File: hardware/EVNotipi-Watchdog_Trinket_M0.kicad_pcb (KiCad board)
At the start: 2 copper layers, 25 x 34 mm, 11 parts, among them J1 Conn_Left, J2 Conn_Right, J3 Conn_Pi, J4 Conn_Pwr, J5 Conn_01x04_Male, Q1 BS170, Q2 IRF5305, U1 TSR_2-2450

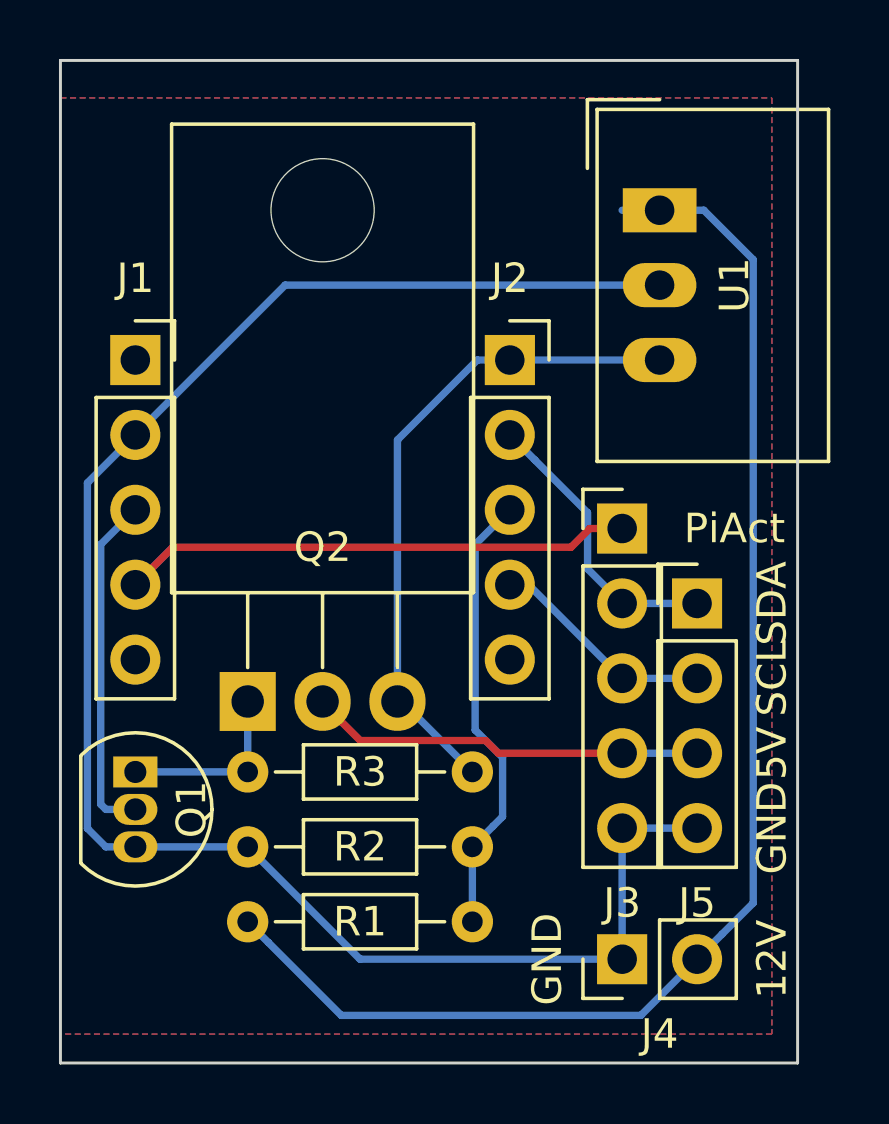
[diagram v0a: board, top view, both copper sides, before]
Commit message: Beef up current carrying traces
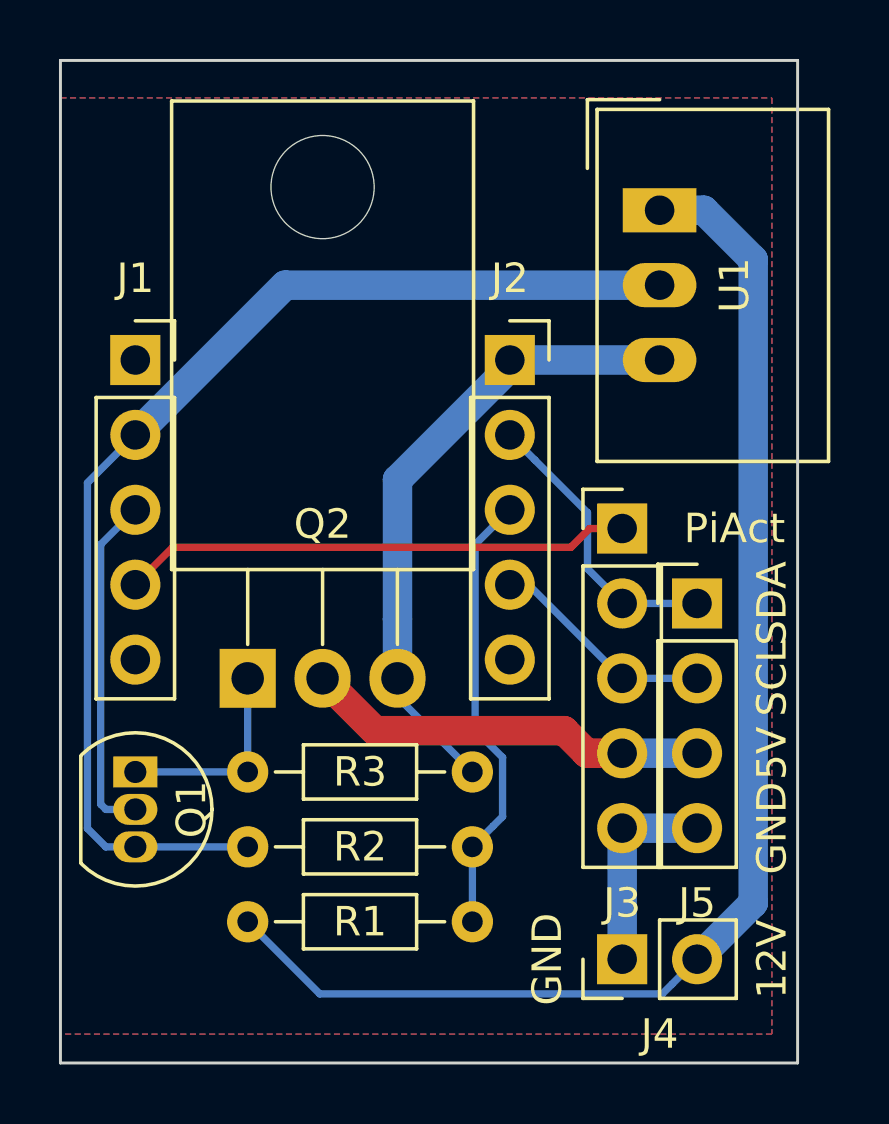
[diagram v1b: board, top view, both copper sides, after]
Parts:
- moved Q2 0.78 mm to (61.0, 51.4)
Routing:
- net GND: track 60.9 -> 46.6 mm
- net VCC12V: track 46.2 -> 45.1 mm
- net Net-(Q1-Pad1): track 6.20 -> 6.98 mm
- net VCC5V: track 22.4 -> 21.7 mm
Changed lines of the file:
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@@
     (thickness 1.6)
     (drawings 11)
-    (tracks 59)
+    (tracks 54)
     (zones 0)
     (modules 11)
@@
   (setup
     (last_trace_width 0.25)
+    (user_trace_width 1)
     (trace_clearance 0.2)
     (zone_clearance 0.508)
@@
   )
   (module Package_TO_SOT_THT:TO-220-3_Horizontal_TabDown (layer F.Cu)
-    (at 60.96 52.22)
+    (at 60.96 51.435)
     (descr "TO-220-3, Horizontal, RM 2.54mm, see https://www.vishay.com/docs/66542/to-220-1.pdf")
     (tags "TO-220-3 Horizontal RM 2.54mm")
@@
   (segment (start 55.974999 46.895001) (end 55.974999 55.704999) (width 0.25) (layer B.Cu) (net 2))
   (segment (start 57.15 45.72) (end 55.974999 46.895001) (width 0.25) (layer B.Cu) (net 2))
-  (segment (start 62.23 38.1) (end 57.15 43.18) (width 0.25) (layer B.Cu) (net 3))
+  (segment (start 62.23 38.1) (end 57.15 43.18) (width 1) (layer B.Cu) (net 3))
   (segment (start 56.15 57.15) (end 57.15 57.15) (width 0.25) (layer B.Cu) (net 3))
   (segment (start 55.524989 56.524989) (end 56.15 57.15) (width 0.25) (layer B.Cu) (net 3))
@@
   (segment (start 57.15 43.18) (end 55.524989 44.805011) (width 0.25) (layer B.Cu) (net 3))
   (segment (start 57.15 57.15) (end 60.96 57.15) (width 0.25) (layer B.Cu) (net 3))
-  (segment (start 64.77 60.96) (end 60.96 57.15) (width 0.25) (layer B.Cu) (net 3))
-  (segment (start 73.66 60.96) (end 64.77 60.96) (width 0.25) (layer B.Cu) (net 3))
-  (segment (start 74.93 38.1) (end 62.23 38.1) (width 0.25) (layer B.Cu) (net 3))
-  (segment (start 74.997919 56.515) (end 73.66 56.515) (width 0.25) (layer B.Cu) (net 3))
-  (segment (start 76.2 56.515) (end 74.997919 56.515) (width 0.25) (layer B.Cu) (net 3))
-  (segment (start 73.66 56.515) (end 73.66 60.96) (width 0.25) (layer B.Cu) (net 3))
+  (segment (start 74.93 38.1) (end 62.23 38.1) (width 1) (layer B.Cu) (net 3))
+  (segment (start 73.66 56.515) (end 73.66 60.96) (width 1) (layer B.Cu) (net 3))
+  (segment (start 73.66 56.515) (end 76.2 56.515) (width 1) (layer B.Cu) (net 3))
   (segment (start 76.2 51.435) (end 73.66 51.435) (width 0.25) (layer B.Cu) (net 4))
   (segment (start 70.485 48.26) (end 69.85 48.26) (width 0.25) (layer B.Cu) (net 4))
@@
   (segment (start 73.66 48.895) (end 72.484999 47.719999) (width 0.25) (layer B.Cu) (net 6))
   (segment (start 73.66 48.895) (end 76.2 48.895) (width 0.25) (layer B.Cu) (net 6))
-  (segment (start 68.75 40.64) (end 69.85 40.64) (width 0.25) (layer B.Cu) (net 7))
-  (segment (start 66.04 43.35) (end 68.75 40.64) (width 0.25) (layer B.Cu) (net 7))
-  (segment (start 66.04 52.22) (end 66.04 43.35) (width 0.25) (layer B.Cu) (net 7))
-  (segment (start 66.19 52.22) (end 66.04 52.22) (width 0.25) (layer B.Cu) (net 7))
-  (segment (start 68.58 54.61) (end 66.19 52.22) (width 0.25) (layer B.Cu) (net 7))
-  (segment (start 74.93 40.64) (end 69.85 40.64) (width 0.25) (layer B.Cu) (net 7))
-  (segment (start 76.2 53.975) (end 73.66 53.975) (width 0.25) (layer B.Cu) (net 8))
-  (segment (start 69.032012 53.54501) (end 64.77751 53.54501) (width 0.25) (layer F.Cu) (net 8))
-  (segment (start 63.5 52.2675) (end 63.5 52.22) (width 0.25) (layer F.Cu) (net 8))
-  (segment (start 64.77751 53.54501) (end 63.5 52.2675) (width 0.25) (layer F.Cu) (net 8))
-  (segment (start 69.462002 53.975) (end 69.032012 53.54501) (width 0.25) (layer F.Cu) (net 8))
-  (segment (start 73.66 53.975) (end 69.462002 53.975) (width 0.25) (layer F.Cu) (net 8))
-  (segment (start 73.66 35.56) (end 74.16 35.56) (width 0.25) (layer B.Cu) (net 9))
-  (segment (start 61.659999 60.389999) (end 60.96 59.69) (width 0.25) (layer B.Cu) (net 9))
-  (segment (start 64.135 62.865) (end 61.659999 60.389999) (width 0.25) (layer B.Cu) (net 9))
-  (segment (start 76.2 60.96) (end 74.295 62.865) (width 0.25) (layer B.Cu) (net 9))
-  (segment (start 74.295 62.865) (end 64.135 62.865) (width 0.25) (layer B.Cu) (net 9))
-  (segment (start 78.105 59.055) (end 77.049999 60.110001) (width 0.25) (layer B.Cu) (net 9))
-  (segment (start 76.43 35.56) (end 78.105 37.235) (width 0.25) (layer B.Cu) (net 9))
-  (segment (start 77.049999 60.110001) (end 76.2 60.96) (width 0.25) (layer B.Cu) (net 9))
-  (segment (start 78.105 37.235) (end 78.105 59.055) (width 0.25) (layer B.Cu) (net 9))
-  (segment (start 74.93 35.56) (end 76.43 35.56) (width 0.25) (layer B.Cu) (net 9))
+  (segment (start 74.93 40.64) (end 69.85 40.64) (width 1) (layer B.Cu) (net 7))
+  (segment (start 66.04 44.695998) (end 66.04 49.435) (width 1) (layer B.Cu) (net 7))
+  (segment (start 69.85 40.885998) (end 66.04 44.695998) (width 1) (layer B.Cu) (net 7))
+  (segment (start 66.04 49.435) (end 66.04 51.435) (width 1) (layer B.Cu) (net 7))
+  (segment (start 69.85 40.64) (end 69.85 40.885998) (width 1) (layer B.Cu) (net 7))
+  (segment (start 66.04 52.07) (end 66.04 51.435) (width 0.25) (layer B.Cu) (net 7))
+  (segment (start 68.58 54.61) (end 66.04 52.07) (width 0.25) (layer B.Cu) (net 7))
+  (segment (start 76.2 53.975) (end 73.66 53.975) (width 1) (layer B.Cu) (net 8))
+  (segment (start 71.692918 53.209999) (end 65.274999 53.209999) (width 1) (layer F.Cu) (net 8))
+  (segment (start 65.274999 53.209999) (end 63.5 51.435) (width 1) (layer F.Cu) (net 8))
+  (segment (start 72.457919 53.975) (end 71.692918 53.209999) (width 1) (layer F.Cu) (net 8))
+  (segment (start 73.66 53.975) (end 72.457919 53.975) (width 1) (layer F.Cu) (net 8))
+  (segment (start 76.43 35.56) (end 78.105 37.235) (width 1) (layer B.Cu) (net 9))
+  (segment (start 78.105 37.235) (end 78.105 59.055) (width 1) (layer B.Cu) (net 9))
+  (segment (start 74.93 35.56) (end 76.43 35.56) (width 1) (layer B.Cu) (net 9))
+  (segment (start 78.105 59.055) (end 76.2 60.96) (width 1) (layer B.Cu) (net 9))
+  (segment (start 75.024999 62.135001) (end 75.350001 61.809999) (width 0.25) (layer B.Cu) (net 9))
+  (segment (start 75.350001 61.809999) (end 76.2 60.96) (width 0.25) (layer B.Cu) (net 9))
+  (segment (start 63.405001 62.135001) (end 75.024999 62.135001) (width 0.25) (layer B.Cu) (net 9))
+  (segment (start 60.96 59.69) (end 63.405001 62.135001) (width 0.25) (layer B.Cu) (net 9))
   (segment (start 57.15 54.61) (end 60.96 54.61) (width 0.25) (layer B.Cu) (net 10))
-  (segment (start 60.96 54.61) (end 60.96 52.22) (width 0.25) (layer B.Cu) (net 10))
+  (segment (start 60.96 54.61) (end 60.96 51.435) (width 0.25) (layer B.Cu) (net 10))
   (zone (net 3) (net_name GND) (layer B.Cu) (hatch edge 0.508)
     (connect_pads (clearance 0.508))
